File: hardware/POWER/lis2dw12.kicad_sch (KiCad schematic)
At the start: 2 parts, among them U2 LIS2DW12

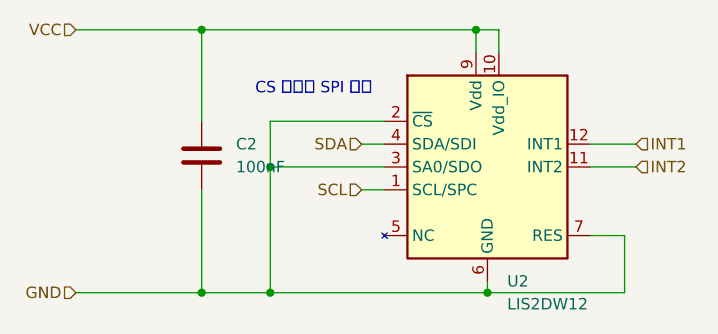
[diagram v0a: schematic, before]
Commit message: lis2dw12由于错误配置了cs脚，导致进入了spi模式，但电路设计上为iic的连接方式，无法读取方向，现在已经修正，但是代码设置成了固定方向。同步升压整流确实降低了不少发热，但是好像添加的ldo由于oled电流较大，带来的额外热量更多，之后可能还是考虑使用dcdc降压
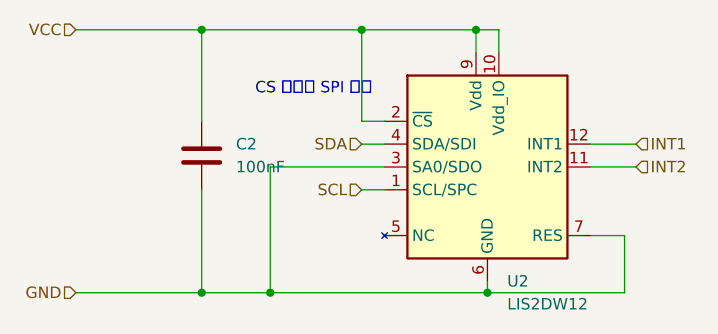
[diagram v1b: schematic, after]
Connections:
- net GND: no longer U2.2 (~{CS})
- net VCC: now also U2.2 (~{CS})
